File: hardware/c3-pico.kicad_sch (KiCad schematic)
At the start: 21 parts, among them J1 USB-C, J2 1x09_Header, J3 1x09_Header, SW1 BOOT, SW2 RESET, U1 ESP32-C3-WROOM-02, U2 AP2112K-3.3, U3 USBLC6-2SC6

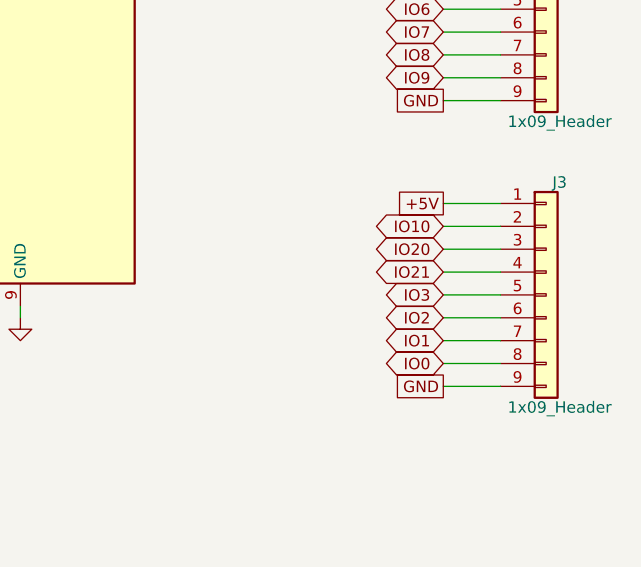
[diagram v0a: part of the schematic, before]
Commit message: Freeze header pinout to module pin order; document placement
Reorder J3 to match the module physical right-side pin order so the
PCB fans out 1:1 without crossings. Update pinout table and status
(placement done: antenna keep-out, USB-C bottom edge, 1.0in rows).
Routing (USB-C differential escape) still in progress.

Co-Authored-By: Claude Opus 4.8 <noreply@anthropic.com>
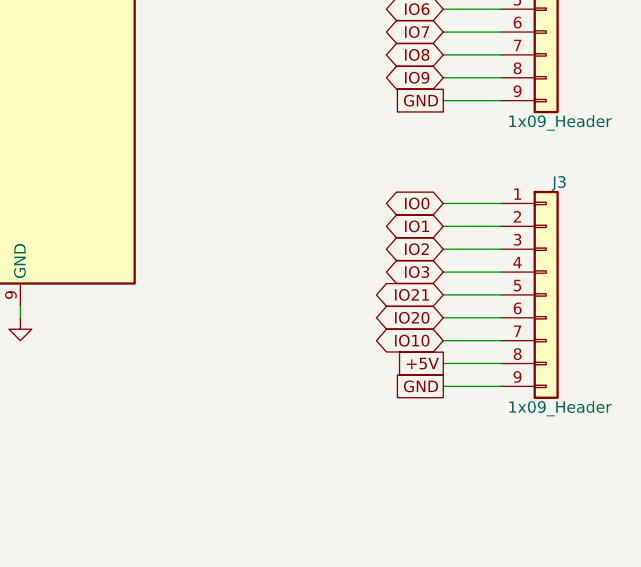
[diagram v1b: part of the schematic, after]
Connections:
- net +5V: now also J3.8 (Pin_8); no longer J3.1 (Pin_1)
- net IO0: now also J3.1 (Pin_1); no longer J3.8 (Pin_8)
- net IO1: now also J3.2 (Pin_2); no longer J3.7 (Pin_7)
- net IO10: now also J3.7 (Pin_7); no longer J3.2 (Pin_2)
- net IO2: now also J3.3 (Pin_3); no longer J3.6 (Pin_6)
- net IO20: now also J3.6 (Pin_6); no longer J3.3 (Pin_3)
- net IO21: now also J3.5 (Pin_5); no longer J3.4 (Pin_4)
- net IO3: now also J3.4 (Pin_4); no longer J3.5 (Pin_5)
